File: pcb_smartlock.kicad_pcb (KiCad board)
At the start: 2 copper layers, 36.7 x 36.7 mm, 57 parts, among them IC1 ST25R3918-AQET, J1 Conn_01x02, J2 Conn_01x03, Q3 IRLML6344TRPBF, Q4 IRLML6344TRPBF, SW1 SKSCLBE010, SW2 SKSCLBE010, SW3 SKSCLBE010, U2 SPX3819M5-L-1-8, U3 ESP32-C3-MINI-1-H4X, U5 SPX3819M5-L-1-8

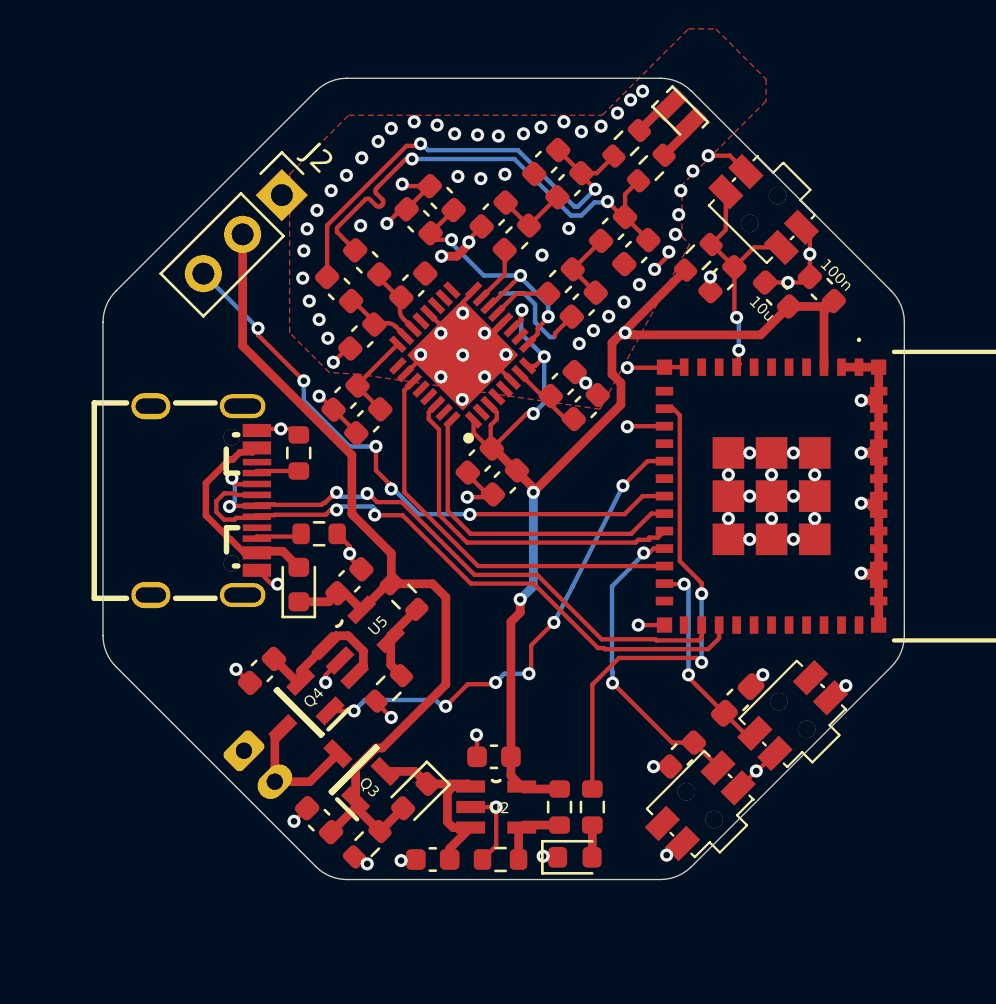
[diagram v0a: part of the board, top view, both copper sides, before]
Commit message: Add silkscreen
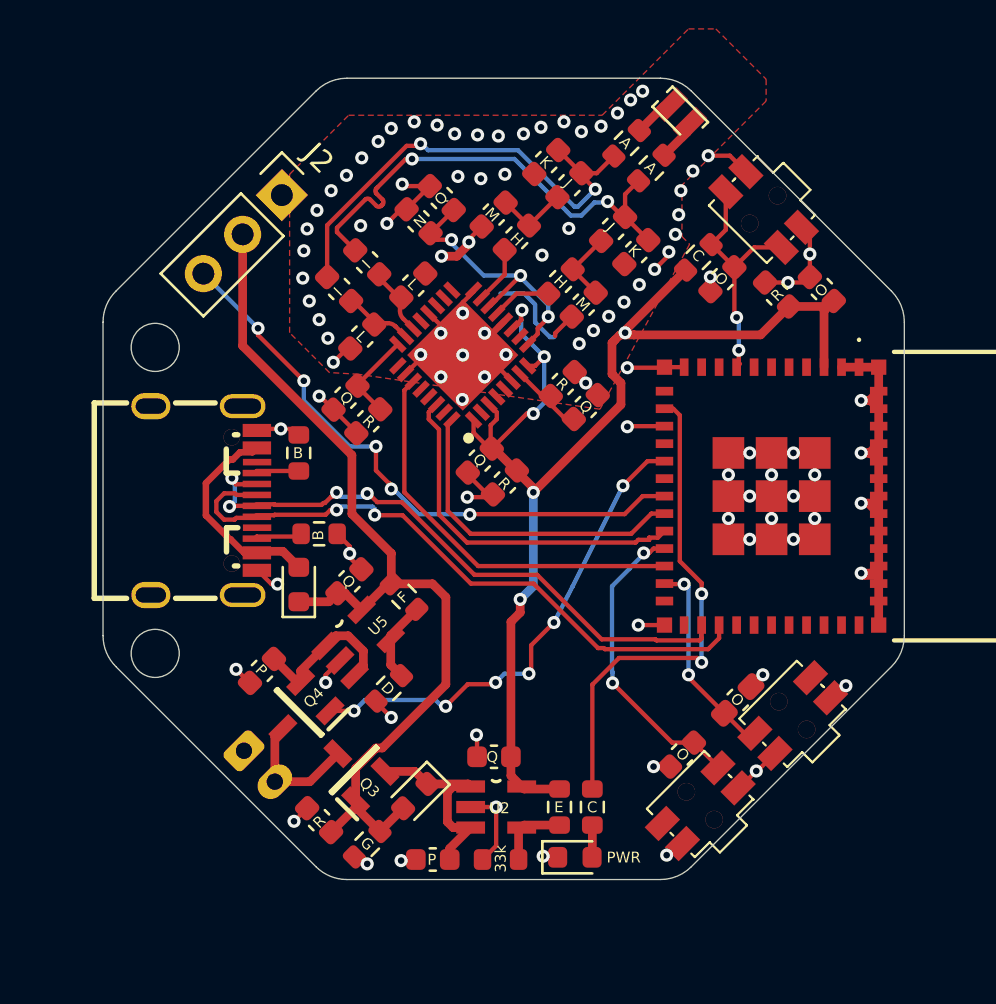
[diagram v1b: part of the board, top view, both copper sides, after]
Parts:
- added REF**: MountingHole_2.2mm_M2, MountingHole:MountingHole_2.2mm_M2, F.Cu at (109.3, 88.2)
- added REF**: MountingHole_2.2mm_M2, MountingHole:MountingHole_2.2mm_M2, F.Cu at (109.3, 102.2)
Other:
- board text added: "33k"
- board text added: "A"
- board text added: "B"
- board text added: "BOOT"
- board text added: "C"
- board text added: "D"
- board text added: "E"
- board text added: "F"
- board text added: "G"
- board text added: "H"
- board text added: "I"
- board text added: "J"
- board text added: "K"
- board text added: "L"
- board text added: "M"
- board text added: "N"
- board text added: "O"
- board text added: "P"
- board text added: "PWR"
- board text added: "Q"
- board text added: "R"
- board text added: "RESET"
- board text added: "SYNC"
- board text removed: "100n"
- board text removed: "10u"

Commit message: correct F.Silkscreen label + add Mouser P/N to all components
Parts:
- U3: value ESP32-C3-MINI-1-H4X -> ESP32-C3-MINI-1-N4X

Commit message: add Interactive BOM HTML
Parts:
- removed REF** (x2): MountingHole_2.2mm_M2, MountingHole:MountingHole_2.2mm_M2
- C10: value 10uf -> 10uF
- C11, C19: value 1uf -> 1uF
- C12: value 10u -> 10uF
- C13: value 100n -> 0.1uF
- C15, C20: value 2.2u -> 2.2uF
- C7, C8: value 0.1u -> 0.1uF
- C9: value 0.1u -> 0.1uF; footprint Capacitor_SMD:C_0603_1608Metric_Pad1.08x0.95mm_HandSolder -> Capacitor_SMD:C_0603_1608Metric
- R4: value 5.1K -> 5.1k
- U3: value ESP32-C3-MINI-1-N4X -> ESP32-C3-MINI-1-H4X
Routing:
- net GND: track 103.7 -> 104.7 mm

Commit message: Edit MOSFET & Schottky to pick available ones
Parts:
- D4, D5: value b5819WS -> SBA130CH-AU_R1_000A1; footprint Diode_SMD:D_0603_1608Metric -> SBA130CH-AU_R1_000A1:SOD-323HE
- U3: value ESP32-C3-MINI-1-H4X -> ESP32-C3-MINI-1-N4X
- moved D5 0.88 mm to (115.8, 99.9)
- moved D4 0.79 mm to (121.8, 108.1)

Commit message: Switch to IRLML0030TRPBF Mosfet (the other were not in stock)
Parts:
- Q3, Q4: value IRLML6344TRPBF -> IRLML0030TRPBF
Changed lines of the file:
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@@
 			)
 		)
-		(property "Value" "IRLML6344TRPBF"
+		(property "Value" "IRLML0030TRPBF "
 			(at 0 0 135)
 			(layer "F.SilkS")
@@
 			)
 		)
-		(property "Datasheet" "https://www.infineon.com/dgdl/irlml6344pbf.pdf?fileId=5546d462533600a4015356689c44262c"
+		(property "Datasheet" "https://www.mouser.fr/datasheet/3/70/1/Infineon_IRLML0030_DataSheet_v01_01_EN.pdf"
 			(at 0 0 135)
 			(layer "F.Fab")
@@
 			)
 		)
-		(property "Mouser Part Number" "942-IRLML6344TRPBF"
-			(at 0 0 135)
-			(unlocked yes)
-			(layer "F.Fab")
-			(hide yes)
-			(effects
-				(font
-					(size 1 1)
-					(thickness 0.15)
-				)
-			)
-		)
-		(property "Mouser Price/Stock" "https://www.mouser.co.uk/ProductDetail/Infineon-Technologies/IRLML6344TRPBF?qs=9%252BKlkBgLFf2w4qS48UOXVw%3D%3D"
+		(property "Mouser Part Number" "942-IRLML0030TRPBF "
+			(at 0 0 135)
+			(unlocked yes)
+			(layer "F.Fab")
+			(hide yes)
+			(effects
+				(font
+					(size 1 1)
+					(thickness 0.15)
+				)
+			)
+		)
+		(property "Mouser Price/Stock" "https://www.mouser.fr/fr/ProductDetail/Infineon-Technologies/IRLML0030TRPBF?qs=9%252BKlkBgLFf0lLJi3xz1alg%3D%3D"
 			(at 0 0 135)
 			(unlocked yes)
@@
 			)
 		)
-		(property "Manufacturer_Part_Number" "IRLML6344TRPBF"
+		(property "Manufacturer_Part_Number" "IRLML0030TRPBF"
 			(at 0 0 135)
 			(unlocked yes)
@@
 			)
 		)
-		(property "Value" "IRLML6344TRPBF"
+		(property "Value" "IRLML0030TRPBF "
 			(at 0 0 45)
 			(layer "F.SilkS")
@@
 			)
 		)
-		(property "Datasheet" "https://www.infineon.com/dgdl/irlml6344pbf.pdf?fileId=5546d462533600a4015356689c44262c"
+		(property "Datasheet" "https://www.mouser.fr/datasheet/3/70/1/Infineon_IRLML0030_DataSheet_v01_01_EN.pdf"
 			(at 0 0 45)
 			(layer "F.Fab")
@@
 			)
 		)
-		(property "Mouser Part Number" "942-IRLML6344TRPBF"
-			(at 0 0 225)
-			(unlocked yes)
-			(layer "F.Fab")
-			(hide yes)
-			(effects
-				(font
-					(size 1 1)
-					(thickness 0.15)
-				)
-			)
-		)
-		(property "Mouser Price/Stock" "https://www.mouser.co.uk/ProductDetail/Infineon-Technologies/IRLML6344TRPBF?qs=9%252BKlkBgLFf2w4qS48UOXVw%3D%3D"
-			(at 0 0 225)
-			(unlocked yes)
+		(property "Mouser Part Number" "942-IRLML0030TRPBF"
+			(at 0 0 225)
+			(unlocked yes)
+			(layer "F.Fab")
+			(hide yes)
+			(effects
+				(font
+					(size 1 1)
+					(thickness 0.15)
+				)
+			)
+		)
+		(property "Mouser Price/Stock" "https://www.mouser.fr/fr/ProductDetail/Infineon-Technologies/IRLML0030TRPBF?qs=9%252BKlkBgLFf0lLJi3xz1alg%3D%3D"
+			(at 0 0 225)
+			(unlocked yes)
